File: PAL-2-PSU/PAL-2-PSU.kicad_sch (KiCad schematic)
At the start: 20 parts, among them J1 Application Connector, J2 +5V, J3 Serial-8, J4 I/O, J5 RS232, SW1 Power, SW2 DECODE_EN, SW3 INPUT, SW4 TTY, U1 MAX202

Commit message: Use 2.54/5.08mm footprint for power switch.
Label Serial-8 pins.
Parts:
- SW1: footprint T-Pau:SS-25139-NH -> T-Pau:SW-2.54-5.08
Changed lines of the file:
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@@
 			)
 		)
-		(property "Footprint" "T-Pau:SS-25139-NH"
+		(property "Footprint" "T-Pau:SW-2.54-5.08"
 			(at 98.425 133.35 0)
 			(effects

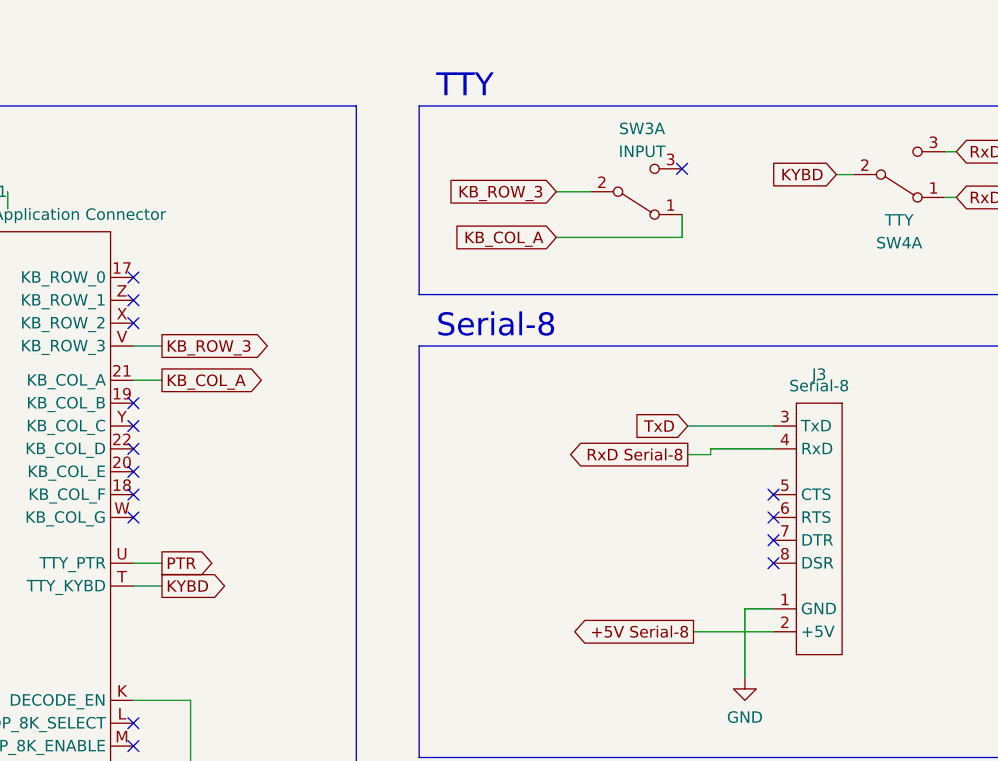
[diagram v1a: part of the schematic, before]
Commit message: Fix missing trace, make switch positions more logical.
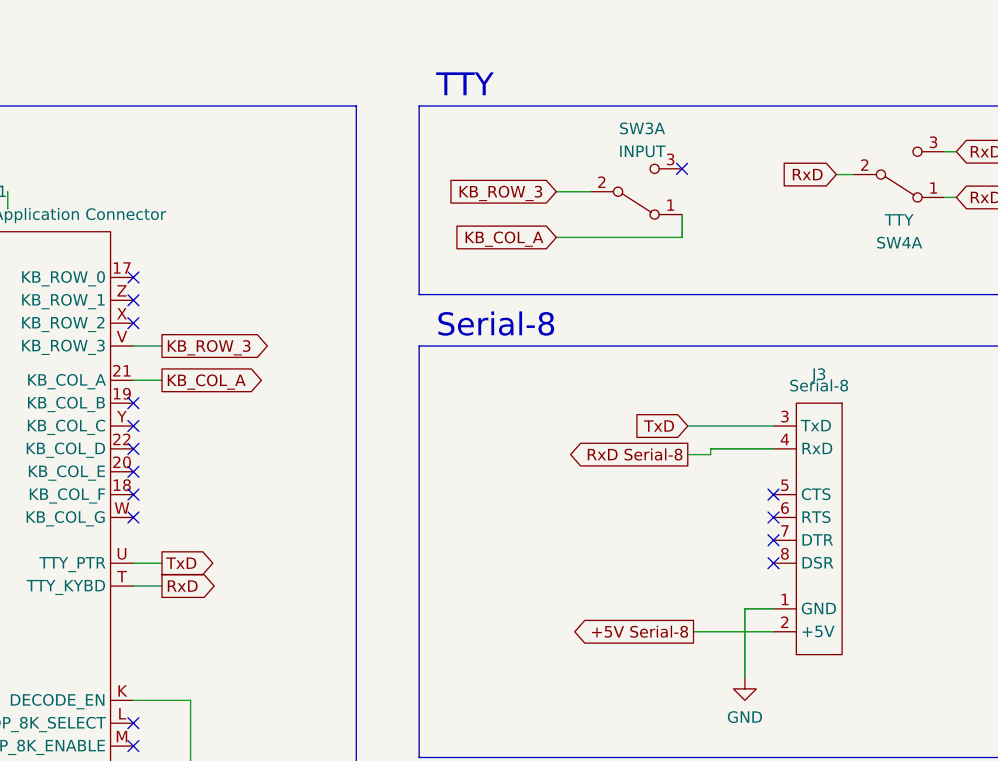
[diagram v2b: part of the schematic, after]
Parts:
- SW1, SW2, SW3, SW4: footprint T-Pau:SW-2.54-5.08 -> T-Pau:SS2513
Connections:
- net PTR is gone; now on net TxD: J1.U (TTY_PTR)
- net KYBD renamed RxD
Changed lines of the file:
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@@
 		)
 	)
-	(global_label "KYBD"
+	(global_label "RxD"
 		(shape input)
 		(at 155.575 29.845 180)
@@
 		)
 		(property "Intersheetrefs" "${INTERSHEET_REFS}"
-			(at 147.6912 29.845 0)
+			(at 149.0217 29.845 0)
 			(effects
 				(font
@@
 		)
 	)
-	(global_label "KYBD"
+	(global_label "RxD"
 		(shape output)
 		(at 80.645 75.565 0)
@@
 		)
 		(property "Intersheetrefs" "${INTERSHEET_REFS}"
-			(at 88.5288 75.565 0)
+			(at 87.1983 75.565 0)
 			(effects
 				(font
@@
 		)
 	)
-	(global_label "PTR"
+	(global_label "TxD"
 		(shape output)
 		(at 80.645 73.025 0)
@@
 		)
 		(property "Intersheetrefs" "${INTERSHEET_REFS}"
-			(at 87.1378 73.025 0)
+			(at 86.8959 73.025 0)
 			(effects
 				(font
@@
 			)
 		)
-		(property "Footprint" "T-Pau:SW-2.54-5.08"
+		(property "Footprint" "T-Pau:SS2513"
 			(at 133.35 31.75 0)
 			(effects
@@
 			)
 		)
-		(property "Footprint" "T-Pau:SW-2.54-5.08"
+		(property "Footprint" "T-Pau:SS2513"
 			(at 83.82 100.965 0)
 			(effects
@@
 			)
 		)
-		(property "Footprint" "T-Pau:SW-2.54-5.08"
+		(property "Footprint" "T-Pau:SS2513"
 			(at 162.56 29.845 0)
 			(effects
@@
 			)
 		)
-		(property "Footprint" "T-Pau:SW-2.54-5.08"
+		(property "Footprint" "T-Pau:SS2513"
 			(at 98.425 133.35 0)
 			(effects
